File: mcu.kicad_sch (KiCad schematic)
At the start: 44 parts, among them J1 Connector, USB-TYPE-C-16P, J201 SWD_3.3V, J202 SWD_GND, J203 SWD_SWDIO, J204 SWD_SWCLK, U1 STM32F723VET6, U2 USBLC6-2SC6, U3 TS3USB221ARSER, U6 SN74AHCT1G125DBVR, X1 16MHz

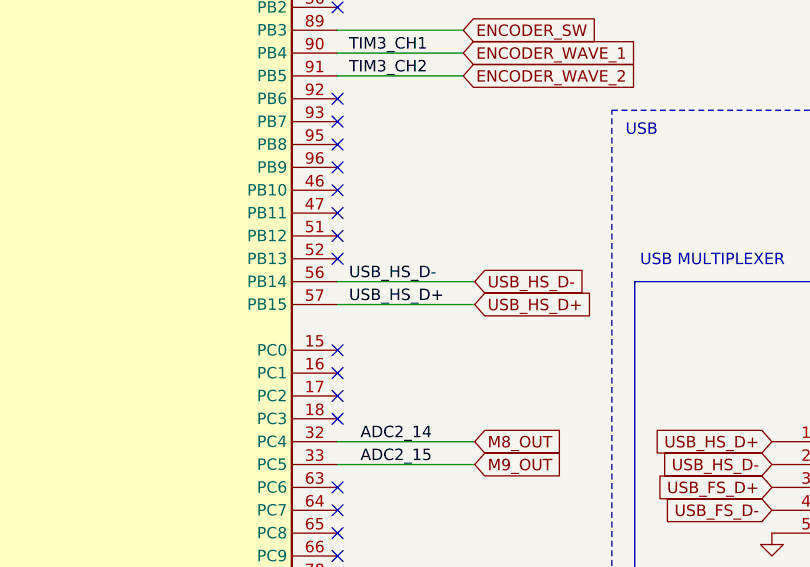
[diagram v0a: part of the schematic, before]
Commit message: mux placement
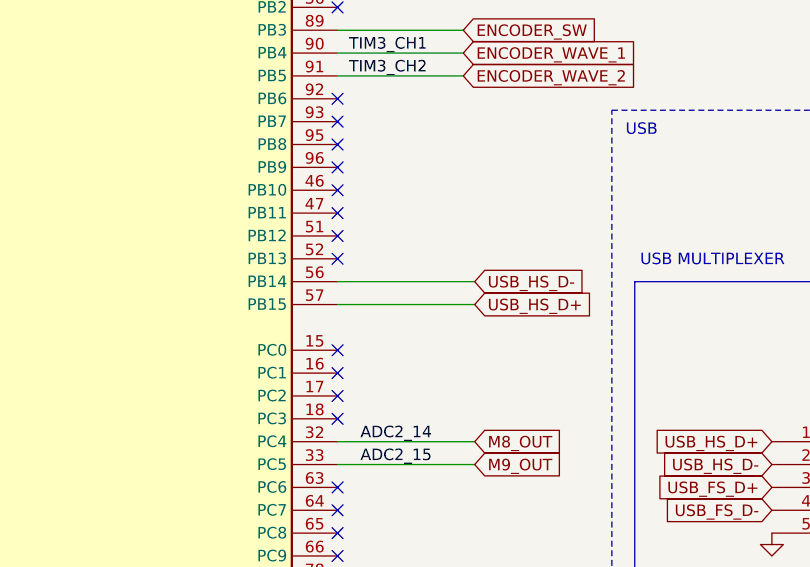
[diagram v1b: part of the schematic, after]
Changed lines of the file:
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@@
-		)
-	)
-	(label "USB_HS_D+"
-		(at 191.77 167.64 0)
-		(effects
-			(font
-				(size 1.27 1.27)
-			)
-			(justify left bottom)
 		)
 	)
@@
 		(effects
 			(font
-				(size 1.27 1.27)
-			)
-			(justify left bottom)
-		)
-	)
-	(label "USB_HS_D-"
-		(at 191.77 165.1 0)
-		(effects
-			(font

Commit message: fix: add missing 3d models
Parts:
- J1: footprint Connector_USB:USB_C_Receptacle_XKB_U262-16XN-4BVC11 -> PCM_JLCPCB:TYPE-C-SMD_HX-TYPE-C-16PIN
- RV1: footprint EC11E15244B2:EC11E15244B2 -> EC11E15244B2; symbol SamacSys_Parts:EC11E15244B2 -> EC11E15244B2:EC11E15244B2
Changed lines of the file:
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@@
 	)
 	(junction
-		(at 392.43 167.64)
-		(diameter 0)
-		(color 0 0 0 0)
-	)
-	(junction
 		(at 154.94 76.2)
 		(diameter 0)
@@
 	)
 	(junction
+		(at 392.43 167.64)
+		(diameter 0)
+		(color 0 0 0 0)
+	)
+	(junction
 		(at 193.04 67.31)
 		(diameter 0)
@@
 	(wire
 		(pts
-			(xy 392.43 167.64) (xy 402.59 167.64)
-		)
-		(stroke
-			(width 0)
-			(type default)
-		)
-	)
-	(wire
-		(pts
 			(xy 172.72 59.69) (xy 180.34 59.69)
 		)
@@
 	(wire
 		(pts
+			(xy 392.43 167.64) (xy 402.59 167.64)
+		)
+		(stroke
+			(width 0)
+			(type default)
+		)
+	)
+	(wire
+		(pts
 			(xy 190.5 139.7) (xy 204.47 139.7)
 		)
@@
 	)
 	(symbol
+		(lib_id "PCM_JLCPCB-Extended:Connector, USB-TYPE-C-16P")
+		(at 384.81 190.5 180)
+		(unit 1)
+		(exclude_from_sim no)
+		(in_bom yes)
+		(on_board yes)
+		(dnp no)
+		(fields_autoplaced yes)
+		(property "Reference" "J1"
+			(at 396.24 190.4999 0)
+			(effects
+				(font
+					(size 1.27 1.27)
+				)
+				(justify right)
+			)
+		)
+		(property "Value" "Connector, USB-TYPE-C-16P"
+			(at 382.27 189.23 0)
+			(effects
+				(font
+					(size 1.27 1.27)
+				)
+				(hide yes)
+			)
+		)
+		(property "Footprint" "PCM_JLCPCB:TYPE-C-SMD_HX-TYPE-C-16PIN"
+			(at 384.81 180.34 0)
+			(effects
+				(font
+					(size 1.27 1.27)
+					(italic yes)
+				)
+				(hide yes)
+			)
+		)
+		(property "Datasheet" "https://atta.szlcsc.com/upload/public/pdf/source/20220920/0EF8F885FCCEA71F60E9E85152155021.pdf"
+			(at 387.096 190.627 0)
+			(effects
+				(font
+					(size 1.27 1.27)
+				)
+				(justify left)
+				(hide yes)
+			)
+		)
+		(property "Description" "3A 1 Horizontal attachment 16P Female -25℃~+85℃ Type-C SMD USB Connectors ROHS"
+			(at 382.27 191.77 0)
+			(effects
+				(font
+					(size 1.27 1.27)
+				)
+				(hide yes)
+			)
+		)
+		(property "LCSC" "C2927039"
+			(at 382.27 191.77 0)
+			(effects
+				(font
+					(size 1.27 1.27)
+				)
+				(hide yes)
+			)
+		)
+		(pin "B8"
+		)
+		(pin "S1"
+		)
+		(pin "A12B1"
+		)
+		(pin "B12A1"
+		)
+		(pin "B7"
+		)
+		(pin "A9B4"
+		)
+		(pin "A7"
+		)
+		(pin "A5"
+		)
+		(pin "A6"
+		)
+		(pin "B9A4"
+		)
+		(pin "B5"
+		)
+		(pin "B6"
+		)
+		(pin "A8"
+		)
+		(instances
+			(project ""
+				(path "/0edb4e17-93a4-4f7b-ad91-3a5c72b69d23/e7ec310e-33d9-421e-aaaf-42ca5ffe1b35"
+					(reference "J1")
+					(unit 1)
+				)
+			)
+		)
+	)
+	(symbol
 		(lib_id "power:GND")
 		(at 193.04 67.31 0)
@@
 	)
 	(symbol
-		(lib_id "PCM_JLCPCB-Extended:Connector, USB-TYPE-C-16P")
-		(at 384.81 190.5 180)
-		(unit 1)
-		(exclude_from_sim no)
-		(in_bom yes)
-		(on_board yes)
-		(dnp no)
-		(fields_autoplaced yes)
-		(property "Reference" "J1"
-			(at 396.24 190.4999 0)
-			(effects
-				(font
-					(size 1.27 1.27)
-				)
-				(justify right)
-			)
-		)
-		(property "Value" "Connector, USB-TYPE-C-16P"
-			(at 382.27 189.23 0)
-			(effects
-				(font
-					(size 1.27 1.27)
-				)
-				(hide yes)
-			)
-		)
-		(property "Footprint" "Connector_USB:USB_C_Receptacle_XKB_U262-16XN-4BVC11"
-			(at 384.81 180.34 0)
-			(effects
-				(font
-					(size 1.27 1.27)
-					(italic yes)
-				)
-				(hide yes)
-			)
-		)
-		(property "Datasheet" "https://atta.szlcsc.com/upload/public/pdf/source/20220920/0EF8F885FCCEA71F60E9E85152155021.pdf"
-			(at 387.096 190.627 0)
-			(effects
-				(font
-					(size 1.27 1.27)
-				)
-				(justify left)
-				(hide yes)
-			)
-		)
-		(property "Description" "3A 1 Horizontal attachment 16P Female -25℃~+85℃ Type-C SMD USB Connectors ROHS"
-			(at 382.27 191.77 0)
-			(effects
-				(font
-					(size 1.27 1.27)
-				)
-				(hide yes)
-			)
-		)
-		(property "LCSC" "C2927039"
-			(at 382.27 191.77 0)
-			(effects
-				(font
-					(size 1.27 1.27)
-				)
-				(hide yes)
-			)
-		)
-		(pin "B5"
-		)
-		(pin "A6"
-		)
-		(pin "A12B1"
-		)
-		(pin "B12A1"
-		)
-		(pin "A5"
-		)
-		(pin "B7"
-		)
-		(pin "A7"
-		)
-		(pin "A8"
-		)
-		(pin "B8"
-		)
-		(pin "S1"
-		)
-		(pin "A9B4"
-		)
-		(pin "B9A4"
-		)
-		(pin "B6"
-		)
-		(instances
-			(project ""
-				(path "/0edb4e17-93a4-4f7b-ad91-3a5c72b69d23/e7ec310e-33d9-421e-aaaf-42ca5ffe1b35"
-					(reference "J1")
-					(unit 1)
-				)
-			)
-			(project "mcu"
-				(path "/acaa5f6a-1300-4933-89e6-4f1ff2a3a17e"
-					(reference "J1")
-					(unit 1)
-				)
-			)
-		)
-	)
-	(symbol
 		(lib_id "Connector:Conn_01x01_Pin")
 		(at 88.9 187.96 180)
@@
 	)
 	(symbol
-		(lib_id "SamacSys_Parts:EC11E15244B2")
+		(lib_id "EC11E15244B2:EC11E15244B2")
 		(at 275.59 111.76 0)
 		(unit 1)
@@
 			)
 		)
-		(property "Footprint" "EC11E15244B2:EC11E15244B2"
+		(property "Footprint" "EC11E15244B2"
 			(at 297.18 199.06 0)
 			(effects

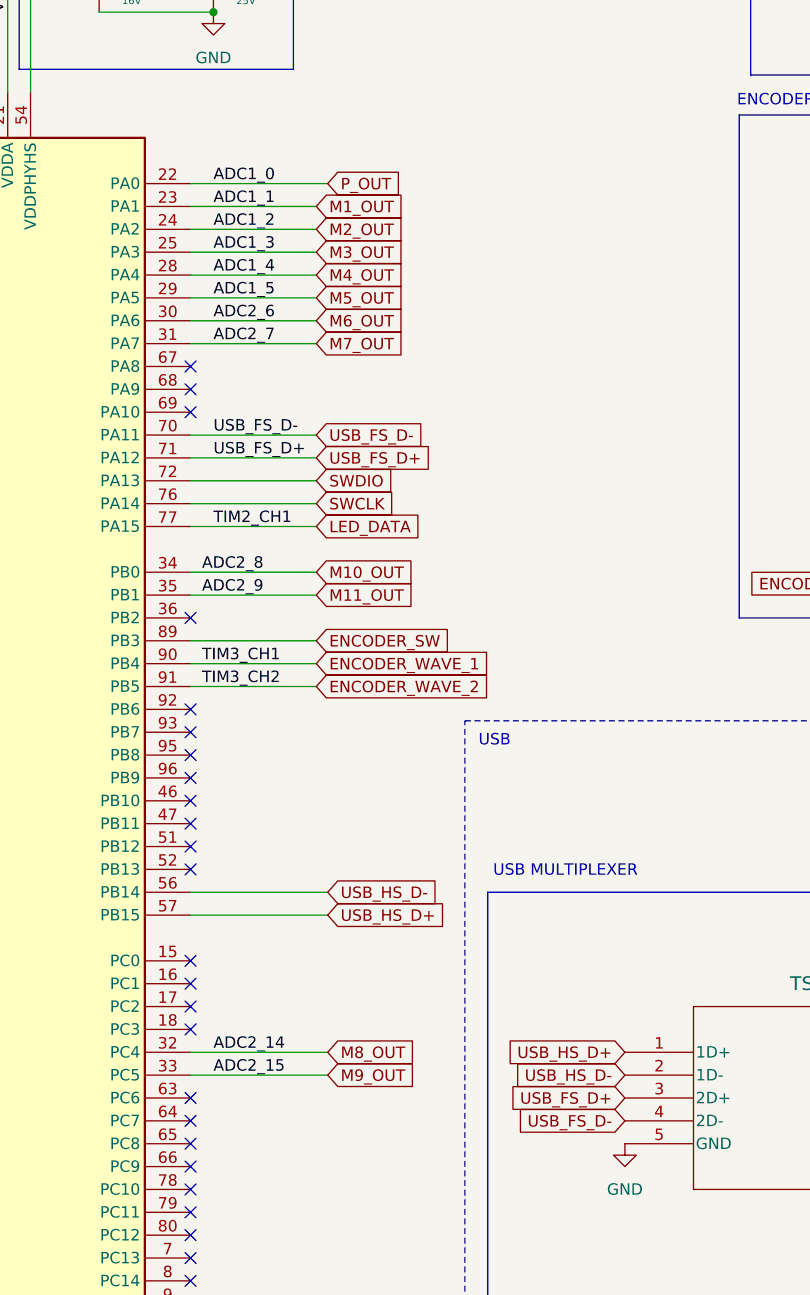
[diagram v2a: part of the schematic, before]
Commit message: mcu capacitor, usb port, ldo
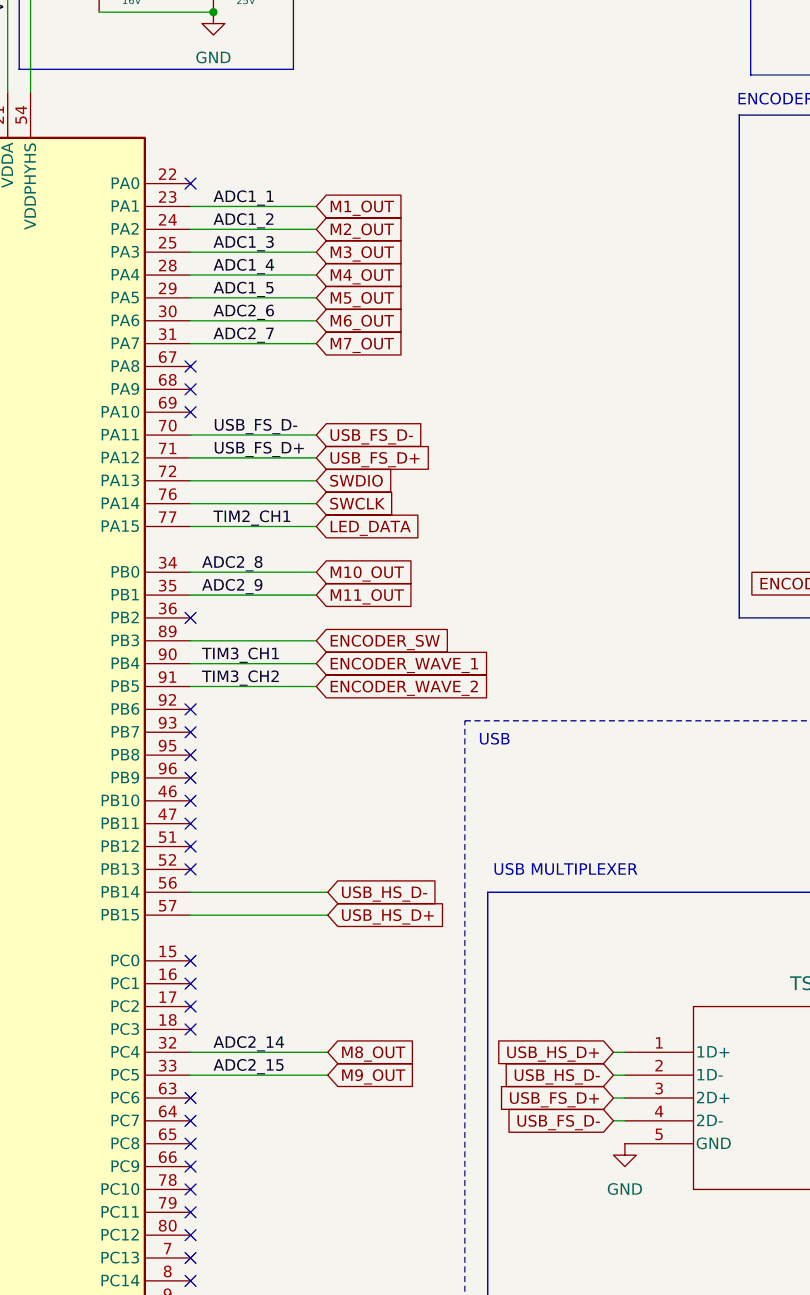
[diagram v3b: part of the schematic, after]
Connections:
- net P_OUT: no longer names the net of U1.22 (PA0)
- no-connect marks 56 -> 57
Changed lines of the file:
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@@
+	)
+	(no_connect
+		(at 190.5 86.36)
 	)
 	(no_connect
@@
 	(wire
 		(pts
-			(xy 190.5 86.36) (xy 205.74 86.36)
-		)
-		(stroke
-			(width 0)
-			(type default)
-		)
-	)
-	(wire
-		(pts
 			(xy 294.64 187.96) (xy 325.12 187.96)
 		)
@@
 	(wire
 		(pts
+			(xy 237.49 185.42) (xy 238.76 185.42)
+		)
+		(stroke
+			(width 0)
+			(type default)
+		)
+	)
+	(wire
+		(pts
 			(xy 78.74 195.58) (xy 83.82 195.58)
 		)
@@
 	(wire
 		(pts
+			(xy 237.49 182.88) (xy 238.76 182.88)
+		)
+		(stroke
+			(width 0)
+			(type default)
+		)
+	)
+	(wire
+		(pts
 			(xy 280.67 95.25) (xy 285.75 95.25)
 		)
@@
 	(wire
 		(pts
+			(xy 237.49 187.96) (xy 238.76 187.96)
+		)
+		(stroke
+			(width 0)
+			(type default)
+		)
+	)
+	(wire
+		(pts
 			(xy 163.83 220.98) (xy 165.1 220.98)
 		)
@@
 		(pts
 			(xy 308.61 58.42) (xy 297.18 58.42)
+		)
+		(stroke
+			(width 0)
+			(type default)
+		)
+	)
+	(wire
+		(pts
+			(xy 237.49 190.5) (xy 238.76 190.5)
 		)
 		(stroke
@@
 	(label "USB_D+"
 		(at 302.26 187.96 0)
-		(effects
-			(font
-				(size 1.27 1.27)
-			)
-			(justify left bottom)
-		)
-	)
-	(label "ADC1_0"
-		(at 193.04 86.36 0)
 		(effects
 			(font
@@
 		)
 	)
-	(global_label "P_OUT"
-		(shape input)
-		(at 205.74 86.36 0)
-		(fields_autoplaced yes)
-		(effects
-			(font
-				(size 1.27 1.27)
-			)
-			(justify left)
-		)
-		(property "Intersheetrefs" "${INTERSHEET_REFS}"
-			(at 214.5914 86.36 0)
-			(effects
-				(font
-					(size 1.27 1.27)
-				)
-				(justify left)
-				(hide yes)
-			)
-		)
-	)
 	(global_label "ENCODER_SW"
 		(shape input)
@@
 	(global_label "USB_HS_D+"
 		(shape input)
-		(at 238.76 182.88 180)
+		(at 237.49 182.88 180)
 		(fields_autoplaced yes)
 		(effects
@@
 		)
 		(property "Intersheetrefs" "${INTERSHEET_REFS}"
-			(at 224.6472 182.88 0)
+			(at 223.3772 182.88 0)
 			(effects
 				(font
@@
 	(global_label "USB_FS_D+"
 		(shape input)
-		(at 238.76 187.96 180)
+		(at 237.49 187.96 180)
 		(fields_autoplaced yes)
 		(effects
@@
 		)
 		(property "Intersheetrefs" "${INTERSHEET_REFS}"
-			(at 224.8891 187.96 0)
+			(at 223.6191 187.96 0)
 			(effects
 				(font
@@
 	(global_label "USB_FS_D-"
 		(shape input)
-		(at 238.76 190.5 180)
+		(at 237.49 190.5 180)
 		(fields_autoplaced yes)
 		(effects
@@
 		)
 		(property "Intersheetrefs" "${INTERSHEET_REFS}"
-			(at 224.8891 190.5 0)
+			(at 223.6191 190.5 0)
 			(effects
 				(font
@@
 	(global_label "USB_HS_D-"
 		(shape input)
-		(at 238.76 185.42 180)
+		(at 237.49 185.42 180)
 		(fields_autoplaced yes)
 		(effects
@@
 		)
 		(property "Intersheetrefs" "${INTERSHEET_REFS}"
-			(at 224.6472 185.42 0)
+			(at 223.3772 185.42 0)
 			(effects
 				(font

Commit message: Placed led
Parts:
- renumbered C178 to C1, C216 to C10, C217 to C11, C176 to C12, C177 to C13, C172 to C14, C173 to C15, C207 to C16, C208 to C17, C215 to C18, C174 to C19, C179 to C2, C175 to C20, C214 to C21, C171 to C3, C170 to C4, C169 to C5, C168 to C6, C167 to C7, C166 to C8, C165 to C9, J201 to J1, J1 to J2, J202 to J3, J203 to J4, J204 to J5, D2 to LED1, R203 to R1, R7 to R2, R287 to R3, R1 to R4, R286 to R5, R288 to R6, R202 to R7, R201 to R8, U6 to U1, U1 to U2, U2 to U4

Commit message: led capacitor & sensor capacitor & fixes
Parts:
- RV1: footprint EC11E15244B2 -> EC11E15244B2:EC11E15244B2
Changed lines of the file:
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@@
 			)
 		)
-		(property "Footprint" "EC11E15244B2"
+		(property "Footprint" "EC11E15244B2:EC11E15244B2"
 			(at 297.18 199.06 0)
 			(hide yes)

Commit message: lcsc part
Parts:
- F1: LCSC (none) -> C1512049
- J1, J3, J4, J5: now left out of the parts list
- RV1: LCSC (none) -> C470754
- SW_BOOT1: value SK-12D02 -> SK-12D02VG3; LCSC (none) -> C131374
- U2: LCSC (none) -> C5270022
- U3: LCSC (none) -> C128396
- U4: LCSC (none) -> C7519
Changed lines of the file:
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@@
 			)
 		)
-		(property "Value" "SK-12D02"
+		(property "Value" "SK-12D02VG3"
 			(at 31.75 85.7249 90)
 			(show_name no)
@@
 			)
 		)
+		(property "LCSC" "C131374"
+			(at 39.37 83.82 90)
+			(hide yes)
+			(show_name no)
+			(do_not_autoplace no)
+			(effects
+				(font
+					(size 1.27 1.27)
+				)
+			)
+		)
 		(pin "2"
 		)
@@
 			)
 		)
+		(property "LCSC" "C7519"
+			(at 330.2 190.5 0)
+			(hide yes)
+			(show_name no)
+			(do_not_autoplace no)
+			(effects
+				(font
+					(size 1.27 1.27)
+				)
+			)
+		)
 		(pin "1"
 		)
@@
 			)
 		)
+		(property "LCSC" "C1512049"
+			(at 353.06 233.68 0)
+			(hide yes)
+			(show_name no)
+			(do_not_autoplace no)
+			(effects
+				(font
+					(size 1.27 1.27)
+				)
+			)
+		)
 		(pin "1"
 		)
@@
 		(body_style 1)
 		(exclude_from_sim no)
-		(in_bom yes)
+		(in_bom no)
 		(on_board yes)
 		(in_pos_files yes)
@@
 		(body_style 1)
 		(exclude_from_sim no)
-		(in_bom yes)
+		(in_bom no)
 		(on_board yes)
 		(in_pos_files yes)
@@
 			)
 		)
+		(property "LCSC" "C128396"
+			(at 238.76 182.88 0)
+			(hide yes)
+			(show_name no)
+			(do_not_autoplace no)
+			(effects
+				(font
+					(size 1.27 1.27)
+				)
+			)
+		)
 		(pin "3"
 		)
@@
 			)
 		)
+		(property "LCSC" "C5270022"
+			(at 162.56 149.86 0)
+			(hide yes)
+			(show_name no)
+			(do_not_autoplace no)
+			(effects
+				(font
+					(size 1.27 1.27)
+				)
+			)
+		)
 		(pin "13"
 		)
@@
 		(body_style 1)
 		(exclude_from_sim no)
-		(in_bom yes)
+		(in_bom no)
 		(on_board yes)
 		(in_pos_files yes)
@@
 		(body_style 1)
 		(exclude_from_sim no)
-		(in_bom yes)
+		(in_bom no)
 		(on_board yes)
 		(in_pos_files yes)
@@
 			)
 		)
+		(property "LCSC" "C470754"
+			(at 275.59 111.76 0)
+			(hide yes)
+			(show_name no)
+			(do_not_autoplace no)
+			(effects
+				(font
+					(size 1.27 1.27)
+				)
+			)
+		)

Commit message: fix
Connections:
- net ENCODER_WAVE_1: now also U2.91 (PB5); no longer U2.90 (PB4)
- net ENCODER_WAVE_2: now also U2.90 (PB4); no longer U2.91 (PB5)

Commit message: Reorganize KiCad libraries; add Legacy Docs
Large repository reorganization of KiCad assets: added Docs and Legacy/ proto directories with many component datasheets and legacy project files, moved and renamed numerous footprints, 3D models and symbol files into consolidated Library/ and Legacy/ paths, and removed outdated/duplicate files. Purpose is to centralize libraries, preserve legacy designs, and clean up footprint/3D model locations for easier maintenance.
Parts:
- U1: footprint SamacSys_Parts:SOT95P280X145-5N -> SN74AHCT1G125DBVR:SOT95P280X145-5N; symbol SamacSys_Parts:SN74AHCT1G125DBVR -> SN74AHCT1G125DBVR:SN74AHCT1G125DBVR
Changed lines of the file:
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@@
 	)
 	(symbol
-		(lib_id "SamacSys_Parts:SN74AHCT1G125DBVR")
+		(lib_id "SN74AHCT1G125DBVR:SN74AHCT1G125DBVR")
 		(at 266.7 55.88 0)
 		(unit 1)
@@
 			)
 		)
-		(property "Footprint" "SamacSys_Parts:SOT95P280X145-5N"
+		(property "Footprint" "SN74AHCT1G125DBVR:SOT95P280X145-5N"
 			(at 288.29 150.8 0)
 			(hide yes)
